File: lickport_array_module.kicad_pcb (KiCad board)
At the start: 2 copper layers, 74.9 x 80.6 mm, 105 parts, among them P1 PWR_JACK_2.1x5.5_SMD_RA, SW1 SPDT_SLIDE_500A_SM, U1 DRV103, U2 DRV103, U3 DRV103, U4 DRV103, U5 DRV103, U6 DRV103, U7 DRV103, U8 DRV103, U9 DRV103

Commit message: Start layout
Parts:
- removed SW1: SPDT_SLIDE_500A_SM, lickport_array_module:SPDT_SLIDE_500A_SM
- added C20: 1uF, lickport_interface:SM0402_POL, F.Cu at (561.7, 52.8)
- added C21: 47nF, lickport_interface:SM0402, F.Cu at (557.0, 59.2)
- added C22: 1uF, lickport_interface:SM0402_POL, F.Cu at (484.4, 136.1)
- added C23: 47nF, lickport_interface:SM0402, F.Cu at (493.4, 123.3)
- added C24: 1uF, lickport_interface:SM0402_POL, F.Cu at (544.7, 84.1)
- added C25: 47nF, lickport_interface:SM0402, F.Cu at (540.0, 90.4)
- added C26: 1uF, lickport_interface:SM0402_POL, F.Cu at (544.7, 115.3)
- added C27: 47nF, lickport_interface:SM0402, F.Cu at (540.0, 121.7)
- added D21: DIODE_SCHOTTKY_0402, lickport_interface:SM0402_POL, F.Cu at (484.8, 130.2)
- added D22: DIODE_LOW_REV_CURRENT_0402, lickport_interface:SM0402_POL, F.Cu at (491.5, 123.6)
- added D23: DIODE_SCHOTTKY_0402, lickport_interface:SM0402_POL, F.Cu at (538.0, 90.7)
- added D24: DIODE_LOW_REV_CURRENT_0402, lickport_interface:SM0402_POL, F.Cu at (537.6, 96.6)
- added D25: DIODE_SCHOTTKY_0402, lickport_interface:SM0402_POL, F.Cu at (538.0, 122.0)
- added D26: DIODE_LOW_REV_CURRENT_0402, lickport_interface:SM0402_POL, F.Cu at (537.6, 127.8)
- added L11: LED_GRN, lickport_interface:LED0805, F.Cu at (476.7, 142.9)
- added L12: LED_GRN, lickport_interface:LED0805, F.Cu at (529.9, 103.4)
- added L13: LED_GRN, lickport_interface:LED0805, F.Cu at (529.9, 134.7)
- added MH10: MOUNTING_HOLE_4-40, lickport_array_module:MOUNTING_HOLE_4-40, F.Cu at (119.7, 143.9)
- added MH11: MOUNTING_HOLE_4-40, lickport_array_module:MOUNTING_HOLE_4-40, F.Cu at (407.9, 23.0)
- added MH12: MOUNTING_HOLE_4-40, lickport_array_module:MOUNTING_HOLE_4-40, F.Cu at (385.4, 40.4)
- added MH13: MOUNTING_HOLE_4-40, lickport_array_module:MOUNTING_HOLE_4-40, F.Cu at (377.3, 53.0)
- added MH14: MOUNTING_HOLE_4-40, lickport_array_module:MOUNTING_HOLE_4-40, F.Cu at (364.7, 60.6)
- added MH4: MOUNTING_HOLE_4-40, lickport_array_module:MOUNTING_HOLE_4-40, F.Cu at (234.7, 33.9)
- added MH5: MOUNTING_HOLE_4-40, lickport_array_module:MOUNTING_HOLE_4-40, F.Cu at (219.7, 58.9)
- added MH6: MOUNTING_HOLE_4-40, lickport_array_module:MOUNTING_HOLE_4-40, F.Cu at (234.7, 88.9)
- added MH7: MOUNTING_HOLE_4-40, lickport_array_module:MOUNTING_HOLE_4-40, F.Cu at (219.7, 118.9)
- added MH8: MOUNTING_HOLE_4-40, lickport_array_module:MOUNTING_HOLE_4-40, F.Cu at (234.7, 143.9)
- added MH9: MOUNTING_HOLE_4-40, lickport_array_module:MOUNTING_HOLE_4-40, F.Cu at (159.7, 143.9)
- added P10: RECEPTACLE_2MM, lickport_interface:RECEPTACLE_2MM, F.Cu at (487.2, 93.9)
- added P11: RECEPTACLE_2MM, lickport_interface:RECEPTACLE_2MM, F.Cu at (557.4, 54.4)
- added P12: RECEPTACLE_2MM, lickport_interface:RECEPTACLE_2MM, F.Cu at (487.2, 125.2)
- added P13: RECEPTACLE_2MM, lickport_interface:RECEPTACLE_2MM, F.Cu at (540.4, 85.7)
- added P14: RECEPTACLE_2MM, lickport_interface:RECEPTACLE_2MM, F.Cu at (540.4, 116.9)
- added P2: BNC, lickport_array_module:BNC, F.Cu at (384.3, 23.8)
- added P3: RECEPTACLE_2MM, lickport_interface:RECEPTACLE_2MM, F.Cu at (380.7, 93.9)
- added P4: RECEPTACLE_2MM, lickport_interface:RECEPTACLE_2MM, F.Cu at (504.2, 23.2)
- added P5: RECEPTACLE_2MM, lickport_interface:RECEPTACLE_2MM, F.Cu at (380.7, 125.2)
- added P6: RECEPTACLE_2MM, lickport_interface:RECEPTACLE_2MM, F.Cu at (433.9, 93.9)
- added P7: RECEPTACLE_2MM, lickport_interface:RECEPTACLE_2MM, F.Cu at (504.2, 54.4)
- added P8: RECEPTACLE_2MM, lickport_interface:RECEPTACLE_2MM, F.Cu at (557.4, 23.2)
- added P9: RECEPTACLE_2MM, lickport_interface:RECEPTACLE_2MM, F.Cu at (433.9, 125.2)
- added R29: 20k, lickport_interface:SM0402, F.Cu at (563.7, 24.1)
- added R30: 137k, lickport_interface:SM0402, F.Cu at (438.3, 126.4)
- added R31: 205k, lickport_interface:SM0402, F.Cu at (440.2, 123.3)
- added R32: 2.2k, lickport_interface:SM0402, F.Cu at (433.5, 129.9)
- added R33: 20k, lickport_interface:SM0402, F.Cu at (423.3, 146.5)
- added R34: 137k, lickport_interface:SM0402, F.Cu at (476.5, 115.3)
- added R35: 205k, lickport_interface:SM0402, F.Cu at (491.5, 95.2)
- added R36: 2.2k, lickport_interface:SM0402, F.Cu at (493.4, 92.0)
- added R37: 20k, lickport_interface:SM0402, F.Cu at (486.8, 98.7)
- added R38: 137k, lickport_interface:SM0402, F.Cu at (563.7, 52.5)
- added R39: 205k, lickport_interface:SM0402, F.Cu at (561.7, 55.7)
- added R40: 2.2k, lickport_interface:SM0402, F.Cu at (546.7, 75.8)
- added R41: 20k, lickport_interface:SM0402, F.Cu at (563.7, 55.4)
- added R42: 137k, lickport_interface:SM0402, F.Cu at (476.5, 146.5)
- added R43: 205k, lickport_interface:SM0402, F.Cu at (493.4, 126.1)
- added R44: 2.2k, lickport_interface:SM0402, F.Cu at (491.5, 126.4)
- added R45: 20k, lickport_interface:SM0402, F.Cu at (486.8, 129.9)
- added R46: 137k, lickport_interface:SM0402, F.Cu at (546.7, 86.6)
- added R47: 205k, lickport_interface:SM0402, F.Cu at (529.7, 107.0)
- added R48: 2.2k, lickport_interface:SM0402, F.Cu at (544.7, 86.9)
- added R49: 20k, lickport_interface:SM0402, F.Cu at (546.7, 83.8)
- added R50: 137k, lickport_interface:SM0402, F.Cu at (546.7, 115.0)
- added R51: 205k, lickport_interface:SM0402, F.Cu at (544.7, 118.2)
- added R52: 2.2k, lickport_interface:SM0402, F.Cu at (529.7, 138.3)
- added R53: 20k, lickport_interface:SM0402, F.Cu at (546.7, 117.9)
- added S10: CLIPPARD-NPV2-1C-23-24, lickport_interface:CLIPPARD_NPV2-1C-23-24, F.Cu at (462.2, 135.2)
- added S11: CLIPPARD-NPV2-1C-23-24, lickport_interface:CLIPPARD_NPV2-1C-23-24, F.Cu at (515.4, 95.7)
- added S12: CLIPPARD-NPV2-1C-23-24, lickport_interface:CLIPPARD_NPV2-1C-23-24, F.Cu at (515.4, 126.9)
- added T1: TERM_BLK_ANG_2_PIN_3.5MM_PITCH, lickport_interface:TERM_BLK_ANG_2_PIN_3.5MM_PITCH, F.Cu at (373.2, 100.0)
- added T10: TERM_BLK_ANG_2_PIN_3.5MM_PITCH, lickport_interface:TERM_BLK_ANG_2_PIN_3.5MM_PITCH, F.Cu at (479.7, 131.3)
- added T11: TERM_BLK_ANG_2_PIN_3.5MM_PITCH, lickport_interface:TERM_BLK_ANG_2_PIN_3.5MM_PITCH, F.Cu at (532.9, 91.8)
- added T12: TERM_BLK_ANG_2_PIN_3.5MM_PITCH, lickport_interface:TERM_BLK_ANG_2_PIN_3.5MM_PITCH, F.Cu at (532.9, 123.0)
- added T2: TERM_BLK_ANG_2_PIN_3.5MM_PITCH, lickport_interface:TERM_BLK_ANG_2_PIN_3.5MM_PITCH, F.Cu at (496.7, 29.3)
- added T3: TERM_BLK_ANG_2_PIN_3.5MM_PITCH, lickport_interface:TERM_BLK_ANG_2_PIN_3.5MM_PITCH, F.Cu at (373.2, 131.3)
- added T4: TERM_BLK_ANG_2_PIN_3.5MM_PITCH, lickport_interface:TERM_BLK_ANG_2_PIN_3.5MM_PITCH, F.Cu at (426.4, 100.0)
- added T5: TERM_BLK_ANG_2_PIN_3.5MM_PITCH, lickport_interface:TERM_BLK_ANG_2_PIN_3.5MM_PITCH, F.Cu at (496.7, 60.5)
- added T6: TERM_BLK_ANG_2_PIN_3.5MM_PITCH, lickport_interface:TERM_BLK_ANG_2_PIN_3.5MM_PITCH, F.Cu at (549.9, 29.3)
- added T7: TERM_BLK_ANG_2_PIN_3.5MM_PITCH, lickport_interface:TERM_BLK_ANG_2_PIN_3.5MM_PITCH, F.Cu at (426.4, 131.3)
- added T8: TERM_BLK_ANG_2_PIN_3.5MM_PITCH, lickport_interface:TERM_BLK_ANG_2_PIN_3.5MM_PITCH, F.Cu at (479.7, 100.0)
- added T9: TERM_BLK_ANG_2_PIN_3.5MM_PITCH, lickport_interface:TERM_BLK_ANG_2_PIN_3.5MM_PITCH, F.Cu at (549.9, 60.5)
- added U10: DRV103, lickport_interface:SOIC_8, F.Cu at (549.7, 66.8)
- added U11: DRV103, lickport_interface:SOIC_8, F.Cu at (479.5, 137.6)
- added U12: DRV103, lickport_interface:SOIC_8, F.Cu at (532.7, 98.1)
- added U13: DRV103, lickport_interface:SOIC_8, F.Cu at (532.7, 129.3)
- C10, C12, C14, C16, C18, C4, C6, C8, D2, R19, R7, U2, U3, U4, U5, U6, U7, U8, U9: moved to F.Cu
- C11, C13, C15, C17, C19, C5, C7, C9: value 15nF -> 47nF; moved to F.Cu
- C2: footprint lickport_interface:SM0402_POL -> lickport_array_module:SM0402_POL; moved to F.Cu
- C3: value 15nF -> 0.1uF; moved to F.Cu
- D10, D12, D14, D16, D18, D20, D4, D6, D8: value DIODE_SCHOTTKY_0402 -> DIODE_LOW_REV_CURRENT_0402; moved to F.Cu
- D11, D13, D15, D17, D19, D3, D5, D7, D9: value DIODE_LOW_REV_CURRENT_0402 -> DIODE_SCHOTTKY_0402; moved to F.Cu
- MH1, MH2, MH3: value VAL** -> MOUNTING_HOLE_4-40; moved to F.Cu
- P1: value PWR_JACK_2.1x5.5_SMD_RA -> PWR_JACK_2.5x5.5_SMD_VERT; footprint lickport_array_module:DCJACK_3PAD_SMD_RA -> lickport_array_module:DCJACK_3PIN_SMD_VERT
- R1, R20, R8: value 390 -> 2.2k; moved to F.Cu
- R10, R22: value 205k -> 137k; moved to F.Cu
- R11, R23: value 390 -> 205k; moved to F.Cu
- R12, R24: value 150k -> 2.2k; moved to F.Cu
- R13, R25: value 205k -> 20k; moved to F.Cu
- R14, R26: value 390 -> 137k; moved to F.Cu
- R15, R27: value 150k -> 205k; moved to F.Cu
- R16, R28: value 205k -> 2.2k; moved to F.Cu
- R17: value 390 -> 20k; moved to F.Cu
- R18, R6: value 150k -> 137k; moved to F.Cu
- R2: value 390 -> 2.2k; footprint lickport_interface:SM0402 -> lickport_array_module:SM0402; moved to F.Cu
- R21, R9: value 150k -> 20k; moved to F.Cu
- R3: value 150k -> 2.2k; footprint lickport_interface:SM0402 -> lickport_array_module:SM0402; moved to F.Cu
- R4: value 205k -> 47k; footprint lickport_interface:SM0402 -> lickport_array_module:SM0402; moved to F.Cu
- R5: value 390 -> 47k; footprint lickport_interface:SM0402 -> lickport_array_module:SM0402; moved to F.Cu
- S1, S2, S3, S4, S5, S6, S7, S8, S9: value VAL** -> CLIPPARD-NPV2-1C-23-24; footprint lickport_interface:LEECO_LHDB -> lickport_interface:CLIPPARD_NPV2-1C-23-24
- TEENSY1: value TEENSY_4.0 -> TEENSY_4.1; footprint lickport_array_module:TEENSY_4.0 -> lickport_array_module:TEENSY_4.1
- U1: value DRV103 -> AT42QT2120-MMHR; footprint lickport_interface:SOIC_8 -> lickport_array_module:QFN-20-1EP_3x3mm_P0.45mm_EP1.6x1.6mm; moved to F.Cu
- moved D13 628.0 mm to (561.7, 21.6), turned to 0 degrees
- moved D14 622.6 mm to (555.0, 28.2), turned to 0 degrees
- moved R26 622.3 mm to (563.7, 21.3), turned to 0 degrees
- moved D19 614.9 mm to (555.0, 59.5), turned to 0 degrees
- moved L7 611.0 mm to (546.9, 40.9)
- moved L10 605.7 mm to (546.9, 72.2)
- moved S6 603.9 mm to (532.4, 33.2), turned to 0 degrees
- moved D6 597.0 mm to (501.4, 34.1), turned to 0 degrees
- moved D20 596.1 mm to (554.6, 65.3), turned to 0 degrees
- moved C6 591.6 mm to (501.8, 28.2), turned to 0 degrees
- moved R27 589.9 mm to (561.7, 24.4), turned to 0 degrees
- moved C14 588.6 mm to (554.6, 34.1), turned to 0 degrees
- moved R10 587.8 mm to (503.8, 27.9), turned to 0 degrees
- moved U3 586.5 mm to (496.5, 35.6), turned to 0 degrees
- moved C15 585.2 mm to (557.0, 27.9), turned to 0 degrees
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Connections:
- C2 pad 1: VCC -> VDD
- C3 pad 1: Net-(C3-Pad1) -> VDD
- D10 pad 1: VCC -> Net-(D10-Pad1)
- D10 pad 2: /odor_3/SH -> VCC
- D11 pad 1: Net-(D11-Pad1) -> VCC
- D11 pad 2: /Vled -> /lickport_interface_4/SH
- D12 pad 1: VCC -> Net-(D12-Pad1)
- D12 pad 2: /odor_4/SH -> VCC
- D13 pad 1: Net-(D13-Pad1) -> VCC
- D13 pad 2: /Vled -> /lickport_interface_5/SH
- D14 pad 1: VCC -> Net-(D14-Pad1)
- D14 pad 2: /odor_5/SH -> VCC
- D15 pad 1: Net-(D15-Pad1) -> VCC
- D15 pad 2: /Vled -> /lickport_interface_6/SH
- D16 pad 1: VCC -> Net-(D16-Pad1)
- D16 pad 2: /odor_6/SH -> VCC
- D17 pad 1: Net-(D17-Pad1) -> VCC
- D17 pad 2: /Vled -> /lickport_interface_7/SH
- D18 pad 1: VCC -> Net-(D18-Pad1)
- D18 pad 2: /odor_7/SH -> VCC
- D19 pad 1: Net-(D19-Pad1) -> VCC
- D19 pad 2: /Vled -> /lickport_interface_8/SH
- D2 pad 2: /Vled -> VCC
- D20 pad 1: VCC -> Net-(D20-Pad1)
- D20 pad 2: /odor_8/SH -> VCC
- D3 pad 1: Net-(D3-Pad1) -> VCC
- D3 pad 2: /Vled -> /lickport_interface_0/SH
- D4 pad 1: VCC -> Net-(D4-Pad1)
- D4 pad 2: /odor_0/SH -> VCC
- D5 pad 1: Net-(D5-Pad1) -> VCC
- D5 pad 2: /Vled -> /lickport_interface_1/SH
- D6 pad 1: VCC -> Net-(D6-Pad1)
- D6 pad 2: /odor_1/SH -> VCC
- D7 pad 1: Net-(D7-Pad1) -> VCC
- D7 pad 2: /Vled -> /lickport_interface_2/SH
- D8 pad 1: VCC -> Net-(D8-Pad1)
- D8 pad 2: /odor_2/SH -> VCC
- D9 pad 1: Net-(D9-Pad1) -> VCC
- D9 pad 2: /Vled -> /lickport_interface_3/SH
- L10 pad 2: /odor_8/SH -> /lickport_interface_8/SH
- L2 pad 2: /odor_0/SH -> /lickport_interface_0/SH
- L3 pad 2: /odor_1/SH -> /lickport_interface_1/SH
- L4 pad 2: /odor_2/SH -> /lickport_interface_2/SH
- L5 pad 2: /odor_3/SH -> /lickport_interface_3/SH
- L6 pad 2: /odor_4/SH -> /lickport_interface_4/SH
- L7 pad 2: /odor_5/SH -> /lickport_interface_5/SH
- L8 pad 2: /odor_6/SH -> /lickport_interface_6/SH
- L9 pad 2: /odor_7/SH -> /lickport_interface_7/SH
- R11 pad 1: Net-(D9-Pad1) -> Net-(R11-Pad1)
- R11 pad 2: Net-(L5-Pad1) -> GND
- R12 pad 1: Net-(R12-Pad1) -> Net-(D6-Pad1)
- R12 pad 2: GND -> Net-(L3-Pad1)
- R13 pad 1: Net-(R13-Pad1) -> Net-(P4-Pad1)
- R13 pad 2: GND -> /TOUCH_1
- R14 pad 1: Net-(D11-Pad1) -> Net-(R14-Pad1)
- R14 pad 2: Net-(L6-Pad1) -> GND
- R16 pad 1: Net-(R16-Pad1) -> Net-(D8-Pad1)
- R16 pad 2: GND -> Net-(L4-Pad1)
- R17 pad 1: Net-(D13-Pad1) -> Net-(P5-Pad1)
- R17 pad 2: Net-(L7-Pad1) -> /TOUCH_2
- R2 pad 1: Net-(D3-Pad1) -> VDD
- R2 pad 2: Net-(L2-Pad1) -> /SDA
- R20 pad 1: Net-(D15-Pad1) -> Net-(D10-Pad1)
- R20 pad 2: Net-(L8-Pad1) -> Net-(L5-Pad1)
- R21 pad 1: Net-(R21-Pad1) -> Net-(P6-Pad1)
- R21 pad 2: GND -> /TOUCH_3
- R23 pad 1: Net-(D17-Pad1) -> Net-(R23-Pad1)
- R23 pad 2: Net-(L9-Pad1) -> GND
- R24 pad 1: Net-(R24-Pad1) -> Net-(D12-Pad1)
- R24 pad 2: GND -> Net-(L6-Pad1)
- R25 pad 1: Net-(R25-Pad1) -> Net-(P7-Pad1)
- R25 pad 2: GND -> /TOUCH_4
- R26 pad 1: Net-(D19-Pad1) -> Net-(R26-Pad1)
- R26 pad 2: Net-(L10-Pad1) -> GND
- R28 pad 1: Net-(R28-Pad1) -> Net-(D14-Pad1)
- R28 pad 2: GND -> Net-(L7-Pad1)
- R3 pad 1: Net-(R3-Pad1) -> VDD
- R3 pad 2: GND -> /SCL
- R4 pad 1: Net-(R4-Pad1) -> VDD
- R4 pad 2: GND -> /~CHANGE
- R5 pad 1: Net-(D5-Pad1) -> VDD
- R5 pad 2: Net-(L3-Pad1) -> Net-(R5-Pad2)
- R8 pad 1: Net-(D7-Pad1) -> Net-(D4-Pad1)
- R8 pad 2: Net-(L4-Pad1) -> Net-(L2-Pad1)
- R9 pad 1: Net-(R9-Pad1) -> Net-(P3-Pad1)
- R9 pad 2: GND -> /TOUCH_0
- TEENSY1 pad 0: (no net) -> /SOLENOID_0
- TEENSY1 pad 12: (no net) -> /~CHANGE
- TEENSY1 pad 14: /ARM_2_ODOR_2 -> /SYNC
- TEENSY1 pad 15: /ARM_2_ODOR_1 -> /SOLENOID_4
- TEENSY1 pad 16: /ARM_2_ODOR_0 -> (no net)
- TEENSY1 pad 17: /ARM_1_ODOR_2 -> (no net)
- TEENSY1 pad 18: /ARM_1_ODOR_1 -> /SDA
- TEENSY1 pad 19: /ARM_1_ODOR_0 -> /SCL
- TEENSY1 pad 20: /ARM_0_ODOR_2 -> /SOLENOID_5
- TEENSY1 pad 21: /ARM_0_ODOR_1 -> (no net)
- TEENSY1 pad 22: /ARM_0_ODOR_0 -> (no net)
- TEENSY1 pad 3: (no net) -> /SOLENOID_1
- TEENSY1 pad 3V3: (no net) -> VDD
- TEENSY1 pad 6: (no net) -> /SOLENOID_2
- TEENSY1 pad 9: (no net) -> /SOLENOID_3
- U1 pad 1: Net-(R3-Pad1) -> /TOUCH_6
- U1 pad 2: Net-(C3-Pad1) -> /TOUCH_5
- U1 pad 3: Net-(R4-Pad1) -> /TOUCH_4
- U1 pad 4: GND -> /TOUCH_3
- U1 pad 5: /odor_0/SH -> /TOUCH_2
- U1 pad 6: VCC -> /TOUCH_1
- U1 pad 7: (no net) -> /TOUCH_0
- U1 pad 8: /ARM_0_ODOR_0 -> GND
- U2 pad 5: /odor_1/SH -> /lickport_interface_0/SH
- U2 pad 8: /ARM_0_ODOR_1 -> /SOLENOID_0
- U3 pad 1: Net-(R9-Pad1) -> Net-(R10-Pad1)
- U3 pad 3: Net-(R10-Pad1) -> Net-(R11-Pad1)
- U3 pad 5: /odor_2/SH -> /lickport_interface_1/SH
- U3 pad 8: /ARM_0_ODOR_2 -> /SOLENOID_1
- U4 pad 1: Net-(R12-Pad1) -> Net-(R14-Pad1)
- U4 pad 3: Net-(R13-Pad1) -> Net-(R15-Pad1)
- U4 pad 5: /odor_3/SH -> /lickport_interface_2/SH
- U4 pad 8: /ARM_1_ODOR_0 -> /SOLENOID_2
- U5 pad 1: Net-(R15-Pad1) -> Net-(R18-Pad1)
- U5 pad 3: Net-(R16-Pad1) -> Net-(R19-Pad1)
- U5 pad 5: /odor_4/SH -> /lickport_interface_3/SH
- U5 pad 8: /ARM_1_ODOR_1 -> /SOLENOID_3
- U6 pad 1: Net-(R18-Pad1) -> Net-(R22-Pad1)
- U6 pad 3: Net-(R19-Pad1) -> Net-(R23-Pad1)
- U6 pad 5: /odor_5/SH -> /lickport_interface_4/SH
- U6 pad 8: /ARM_1_ODOR_2 -> /SOLENOID_4
- U7 pad 1: Net-(R21-Pad1) -> Net-(R26-Pad1)
- U7 pad 3: Net-(R22-Pad1) -> Net-(R27-Pad1)
- U7 pad 5: /odor_6/SH -> /lickport_interface_5/SH
- U7 pad 8: /ARM_2_ODOR_0 -> /SOLENOID_5
- U8 pad 1: Net-(R24-Pad1) -> Net-(R30-Pad1)
- U8 pad 3: Net-(R25-Pad1) -> Net-(R31-Pad1)
- U8 pad 5: /odor_7/SH -> /lickport_interface_6/SH
- U8 pad 8: /ARM_2_ODOR_1 -> /SOLENOID_6
- U9 pad 1: Net-(R27-Pad1) -> Net-(R34-Pad1)
- U9 pad 3: Net-(R28-Pad1) -> Net-(R35-Pad1)
- U9 pad 5: /odor_8/SH -> /lickport_interface_7/SH
- U9 pad 8: /ARM_2_ODOR_2 -> /SOLENOID_7
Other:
- board size 74.9 x 80.6 mm -> 203.2 x 147.3 mm
- board text added: "2.5x5.5 Center + +24VDC"
- board text removed: "0"
- board text removed: "1"
- board text removed: "2"
- board text removed: "2.1x5.5 Center + +12VDC"
- board text removed: "ARM"
- board text removed: "ARM 0"
- board text removed: "ARM 1"
- board text removed: "ARM 2"
- board text removed: "ODOR"
- board text removed: "ODOR 0"
- board text removed: "ODOR 1"
- board text removed: "ODOR 2"

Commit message: Lay out solenoids
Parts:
- moved C26 514.4 mm to (30.3, 120.4)
- moved C27 514.4 mm to (25.6, 126.8)
- moved D25 514.4 mm to (23.7, 127.1)
- moved D26 514.4 mm to (23.3, 132.9)
- moved L13 514.4 mm to (15.6, 139.8)
- moved R50 514.4 mm to (32.3, 120.1)
- moved R51 514.4 mm to (30.3, 123.3)
- moved R53 514.4 mm to (32.3, 123.0)
- moved T12 514.4 mm to (18.5, 128.1)
- moved U13 514.4 mm to (18.3, 134.4)
- moved R52 514.4 mm to (15.4, 143.3)
- moved P13 490.1 mm to (54.0, 146.1)
- moved C25 471.1 mm to (76.4, 174.3)
- moved D23 471.1 mm to (74.5, 174.6)
- moved D24 471.1 mm to (74.1, 180.4)
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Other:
- board text added: "0"
- board text added: "1"
- board text added: "10"
- board text added: "11"
- board text added: "2"
- board text added: "3"
- board text added: "4"
- board text added: "5"
- board text added: "6"
- board text added: "7"
- board text added: "8"
- board text added: "9"

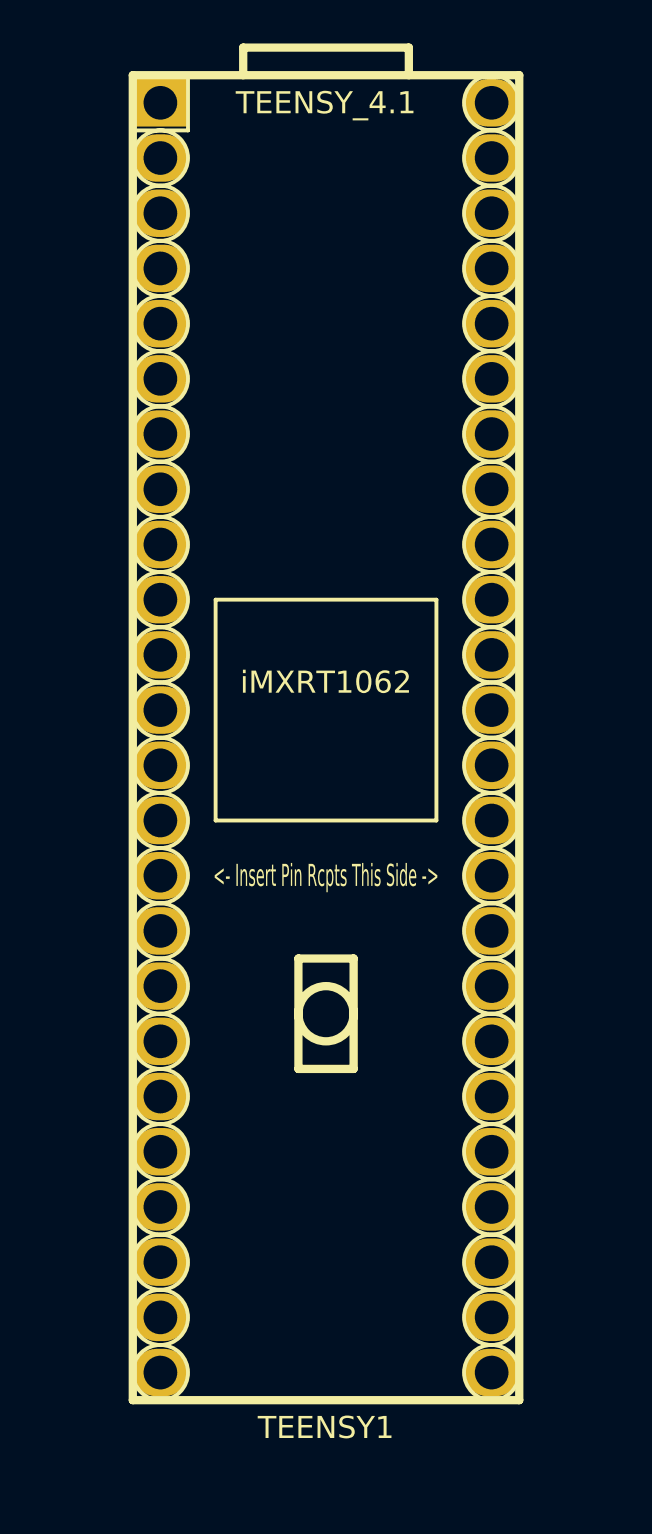
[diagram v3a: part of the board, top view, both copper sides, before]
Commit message: Switch Teensy connection from pin receptacles to headers
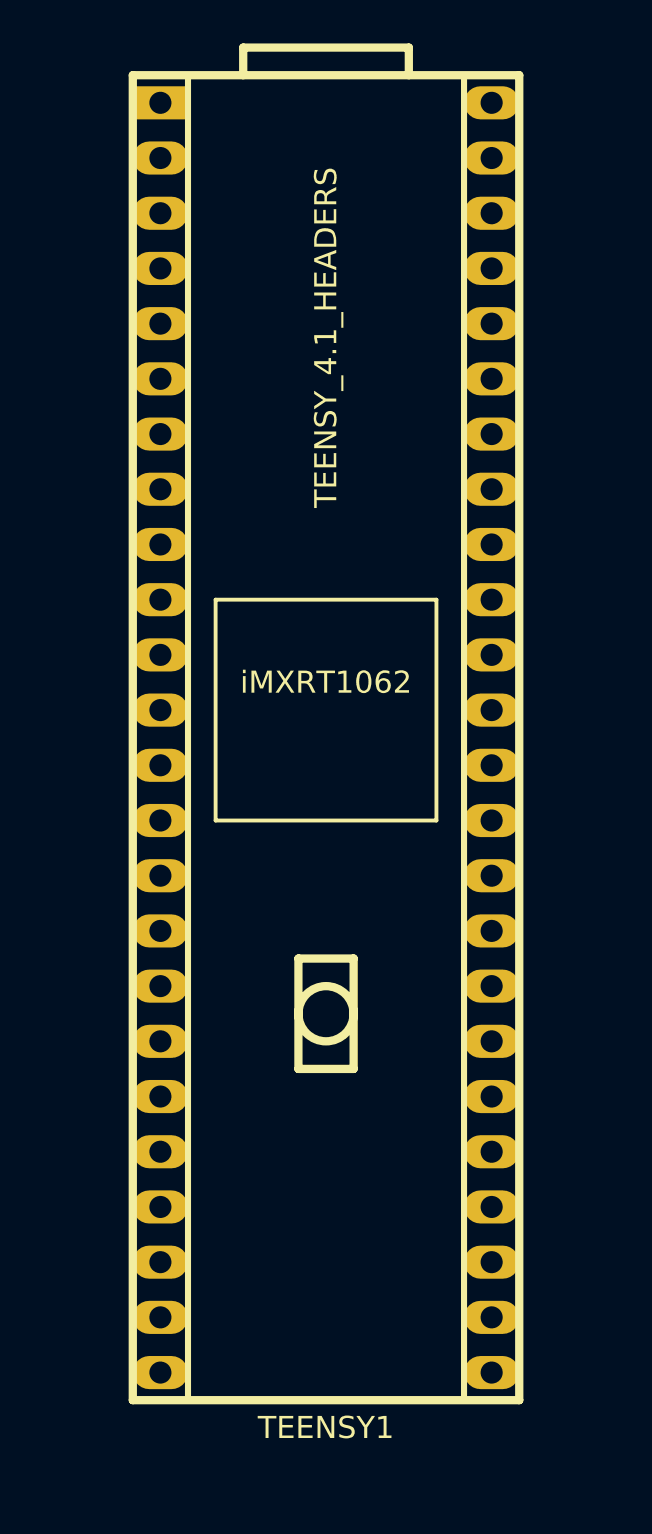
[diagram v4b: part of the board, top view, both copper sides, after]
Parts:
- TEENSY1: value TEENSY_4.1 -> TEENSY_4.1_HEADERS; footprint lickport_array_module:TEENSY_4.1 -> lickport_array_module:TEENSY_4.1_HEADERS

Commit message: Completed initial layout
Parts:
- moved R4 293.5 mm to (143.5, 159.4), turned to 180 degrees
- moved R5 286.5 mm to (137.8, 159.4), turned to 180 degrees
- moved C1 266.9 mm to (130.8, 56.5)
- moved D1 265.8 mm to (130.8, 48.3)
- moved R2 255.1 mm to (135.9, 159.4), turned to 180 degrees
- moved L1 254.3 mm to (139.8, 18.4)
- moved R3 251.7 mm to (141.6, 159.4), turned to 180 degrees
- moved D2 250.6 mm to (143.5, 18.4)
- moved P1 238.0 mm to (130.8, 33.0), turned to 180 degrees
- moved P2 236.4 mm to (148.0, 27.9)
- moved C3 235.4 mm to (133.3, 156.8), turned to 90 degrees
- moved C2 232.8 mm to (133.3, 154.9), turned to 90 degrees
- moved R1 222.7 mm to (141.6, 18.4)
- moved TEENSY1 196.3 mm to (139.7, 82.5)
- moved R25 169.5 mm to (139.7, 146.7)
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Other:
- net class Default: clearance 0.2 -> 0.1016; trace_width 0.25 -> 0.4064; via_dia 0.8 -> 0.889; via_drill 0.4 -> 0.635
- net class SIGNAL added: clearance 0.1016, trace_width 0.4064, via_dia 0.889, via_drill 0.635
- rule trace_clearance: 0.2 -> 0.1016

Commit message: Initial routing
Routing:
- net GND: track 0.00 -> 837.2 mm
- net VCC: track 0.00 -> 832.7 mm
- net Net-(P4-Pad1): track 0.00 -> 151.9 mm, vias 0 -> 1
- net Net-(P7-Pad1): track 0.00 -> 149.9 mm, vias 0 -> 1
- net Net-(P6-Pad1): track 0.00 -> 127.1 mm, vias 0 -> 1
- net Net-(P3-Pad1): track 0.00 -> 125.2 mm, vias 0 -> 1
- net Net-(P5-Pad1): track 0.00 -> 124.7 mm, vias 0 -> 1
- net /SOLENOID_4: track 0.00 -> 116.4 mm, vias 0 -> 1
- net VDD: track 0.00 -> 112.7 mm, vias 0 -> 2
- net /SOLENOID_10: track 0.00 -> 110.9 mm
- net Net-(P8-Pad1): track 0.00 -> 107.5 mm, vias 0 -> 1
- net /SOLENOID_7: track 0.00 -> 104.0 mm
- net Net-(P13-Pad1): track 0.00 -> 102.9 mm
- net /SOLENOID_3: track 0.00 -> 95.3 mm, vias 0 -> 1
- net /SOLENOID_0: track 0.00 -> 93.7 mm
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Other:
- net class POWER: trace_width 0.4064 -> 0.2032; via_dia 0.889 -> 0.8128; via_drill 0.635 -> 0.4064
- net class SIGNAL: trace_width 0.4064 -> 0.2032; via_dia 0.889 -> 0.8128; via_drill 0.635 -> 0.4064
